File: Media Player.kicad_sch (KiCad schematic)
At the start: 71 parts, among them J1 PH2.0, J2 MEM2075-00-140-01-A, J3 USB_C_Receptacle_USB2.0_14P, J4 UART, Q2 DMP3068L-7, Q3 DMP3068L-7, SW1 BOOT, SW2 RESET, SW3 SW_Push, SW4 SW_Push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

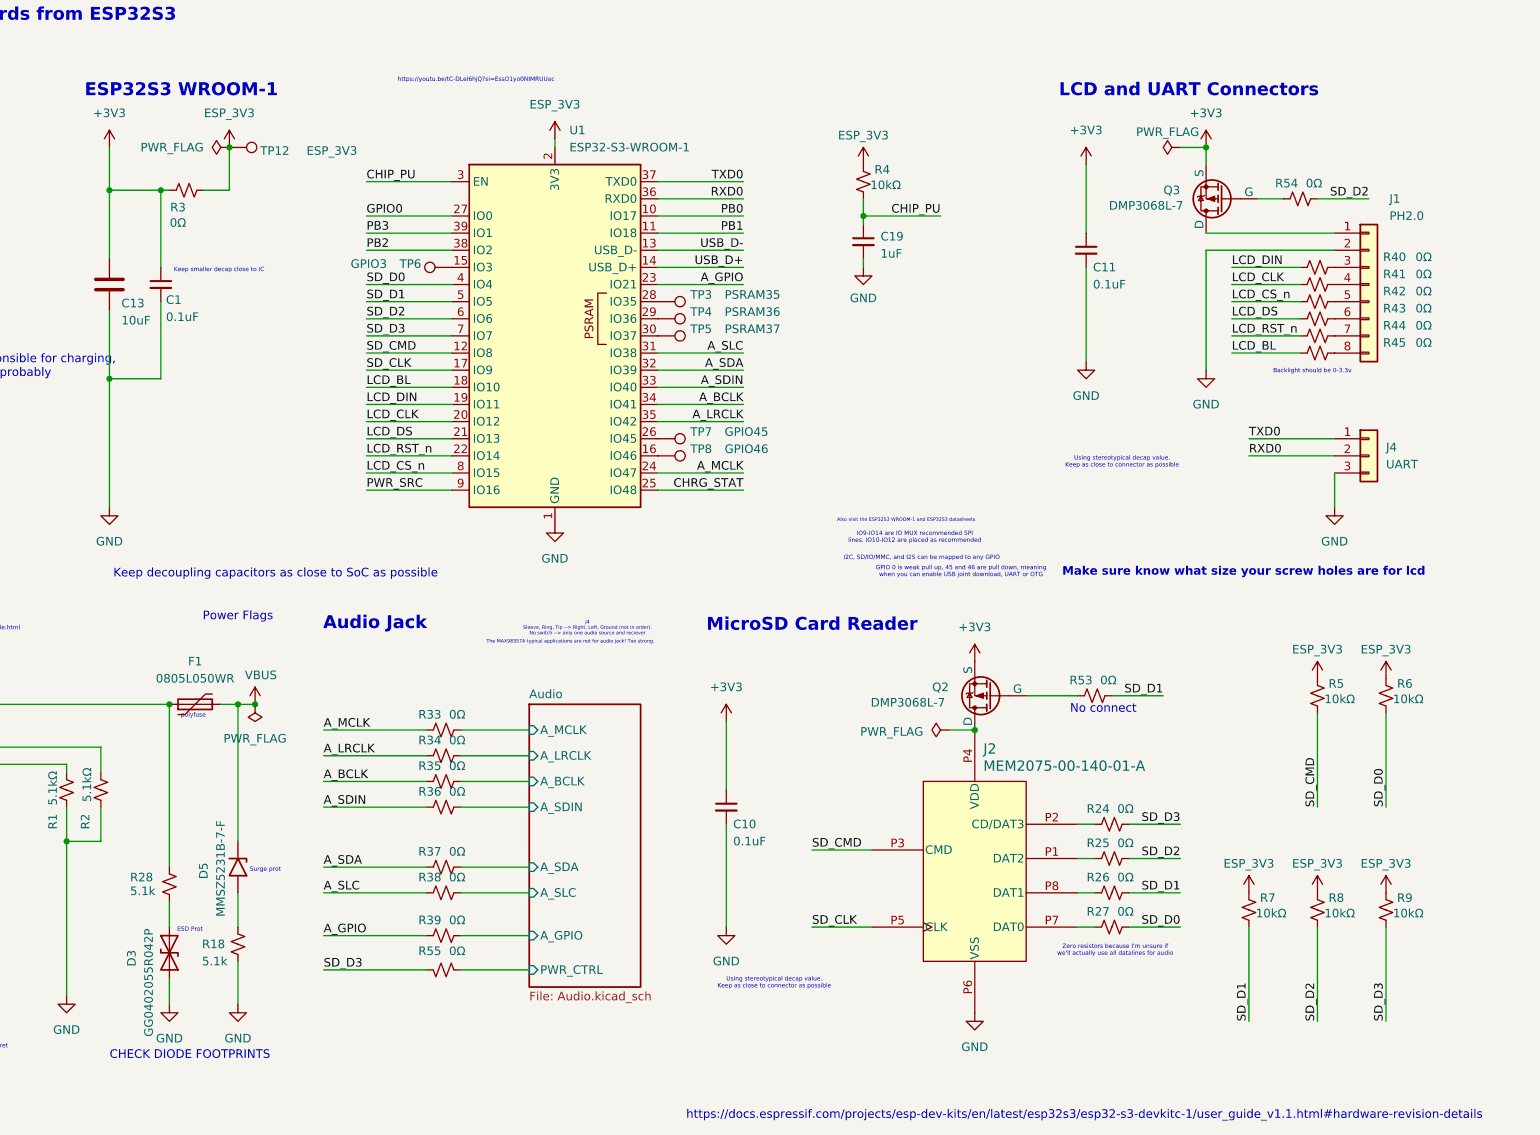
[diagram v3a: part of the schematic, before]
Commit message: Ratsnest organized
Certain pins on esp32 module changed to benefit layout. Named all decaps to dC. Current layout areas might be not optimal, i.e. complicated to wire
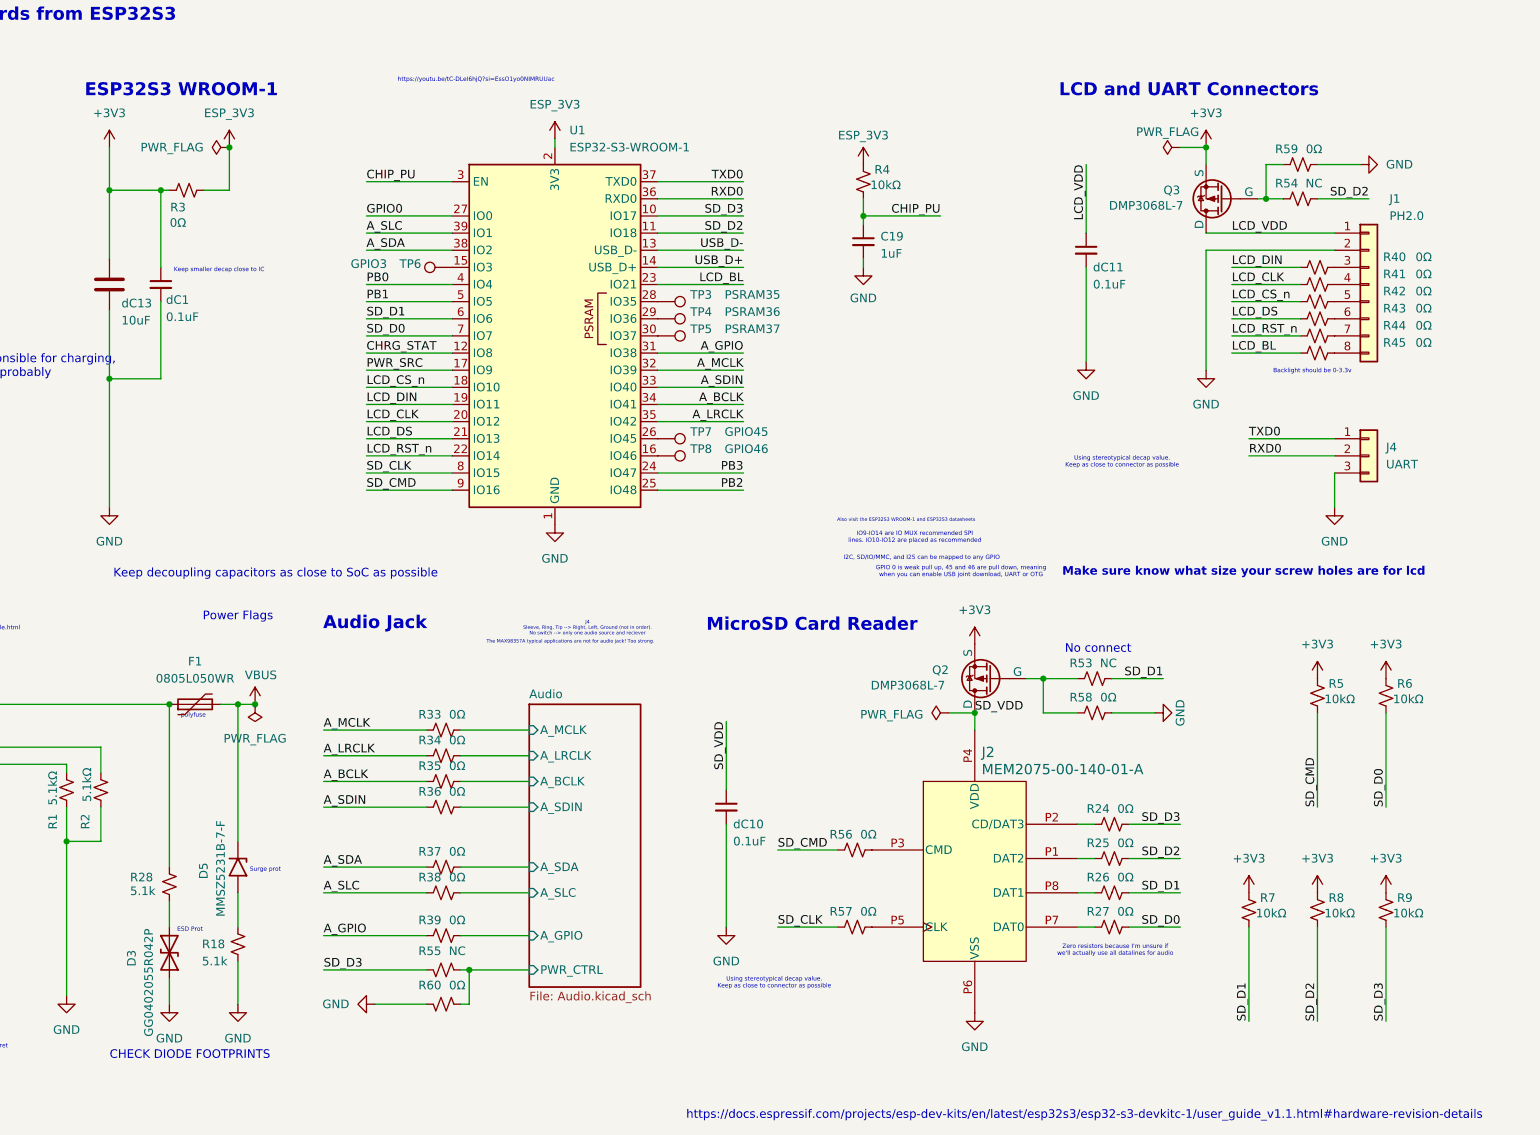
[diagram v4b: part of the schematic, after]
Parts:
- removed TP12: ESP_3V3, TestPoint:TestPoint_Pad_1.5x1.5mm, symbol Connector:TestPoint
- added R56, R57, R58, R59, R60: 0Ω, Resistor_SMD:R_0805_2012Metric, symbol Device:R_Small_US
- C19: footprint Capacitor_SMD:C_0805_2012Metric_Pad1.18x1.45mm_HandSolder -> Capacitor_SMD:C_0603_1608Metric_Pad1.08x0.95mm_HandSolder
- R53, R54, R55: value 0Ω -> NC
- dC1: renamed from C1; footprint Capacitor_SMD:C_0805_2012Metric_Pad1.18x1.45mm_HandSolder -> Capacitor_SMD:C_0603_1608Metric_Pad1.08x0.95mm_HandSolder
- dC10: renamed from C10; footprint Capacitor_SMD:C_0805_2012Metric_Pad1.18x1.45mm_HandSolder -> Capacitor_SMD:C_0603_1608Metric_Pad1.08x0.95mm_HandSolder
- dC11: renamed from C11; footprint Capacitor_SMD:C_0805_2012Metric_Pad1.18x1.45mm_HandSolder -> Capacitor_SMD:C_0603_1608Metric_Pad1.08x0.95mm_HandSolder
- dC13: renamed from C13; footprint Capacitor_SMD:C_0805_2012Metric_Pad1.18x1.45mm_HandSolder -> Capacitor_SMD:C_0603_1608Metric_Pad1.08x0.95mm_HandSolder
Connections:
- net +3V3: now also R5.2, R6.2, R7.2, R8.2, R9.2; no longer dC10.1, dC11.1
- net A_GPIO: now also U1.31 (IO38); no longer U1.23 (IO21)
- net A_MCLK: now also U1.32 (IO39); no longer U1.24 (IO47)
- net A_SDA: now also U1.38 (IO2); no longer U1.32 (IO39)
- net A_SLC: now also U1.39 (IO1); no longer U1.31 (IO38)
- net Audio/PWR_CTRL: now also R60.1
- net CHRG_STAT: now also U1.12 (IO8); no longer U1.25 (IO48)
- net ESP_3V3: no longer R5.2, R6.2, R7.2, R8.2, R9.2
- net GND: now also R58.2, R59.2, R60.2
- net LCD_BL: now also U1.23 (IO21); no longer U1.18 (IO10)
- net LCD_CS_n: now also U1.18 (IO10); no longer U1.8 (IO15)
- net PB0: now also U1.4 (IO4); no longer U1.10 (IO17)
- net PB1: now also U1.5 (IO5); no longer U1.11 (IO18)
- net PB2: now also U1.25 (IO48); no longer U1.38 (IO2)
- net PB3: now also U1.24 (IO47); no longer U1.39 (IO1)
- net PWR_SRC: now also U1.17 (IO9); no longer U1.9 (IO16)
- net SD_CLK: now also U1.8 (IO15), R57.1; no longer J2.P5 (CLK), U1.17 (IO9)
- net SD_CMD: now also U1.9 (IO16), R56.1; no longer J2.P3 (CMD), U1.12 (IO8)
- net SD_D0: now also U1.7 (IO7); no longer U1.4 (IO4)
- net SD_D1: now also U1.6 (IO6); no longer U1.5 (IO5)
- net SD_D2: now also U1.11 (IO18); no longer U1.6 (IO6)
- net SD_D3: now also U1.10 (IO17); no longer U1.7 (IO7)
- net SD_VDD: now reaches J2.P4 (VDD), Q2.1 (D)
- net SD_VDD: now also dC10.1
- net at Q2.2 (G), R53.1: now also R58.1
- net at Q3.2 (G), R54.1: now also R59.1
- net LCD_VDD: now reaches J1.1 (Pin_1), Q3.1 (D)
- net LCD_VDD: now also dC11.1
- new net: J2.P3 (CMD), R56.2
- new net: J2.P5 (CLK), R57.2
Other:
- moved on the sheet: Q2, R53

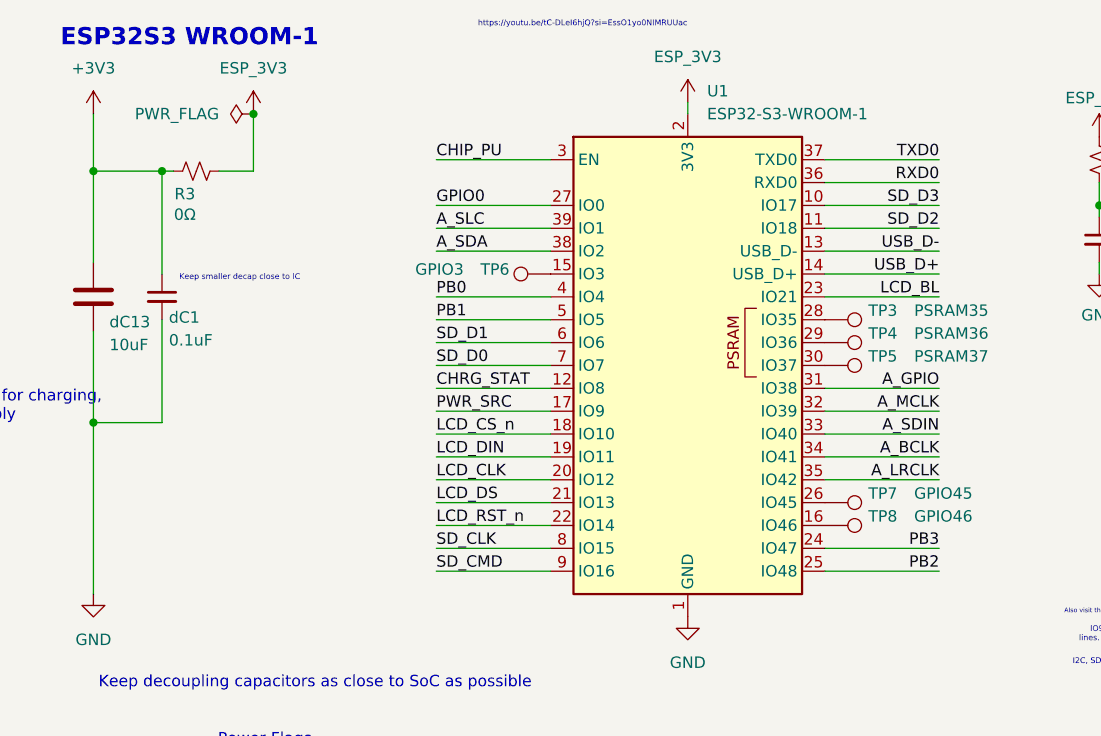
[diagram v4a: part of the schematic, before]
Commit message: Component Re-order
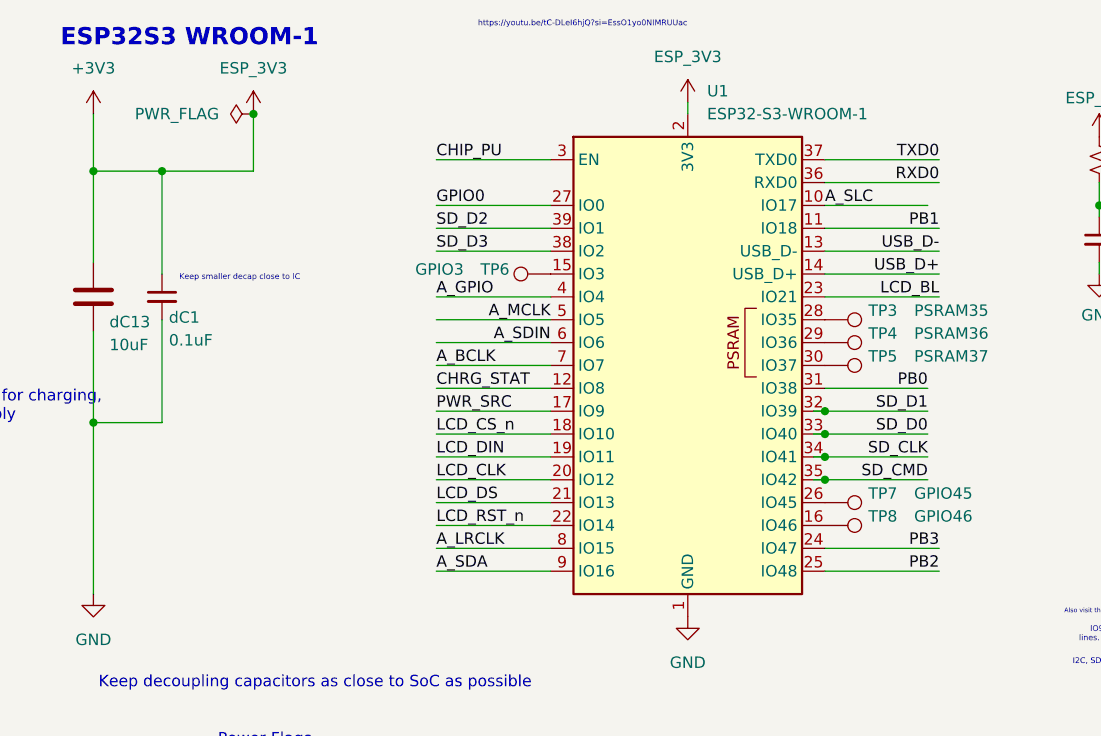
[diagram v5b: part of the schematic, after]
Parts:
- removed R3: 0Ω, Resistor_SMD:R_0805_2012Metric, symbol Device:R_Small_US
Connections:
- net ESP_3V3 is gone; now on net +3V3: R4.2, U1.2 (3V3)
- net A_BCLK: now also U1.7 (IO7); no longer U1.34 (IO41)
- net A_GPIO: now also U1.4 (IO4); no longer U1.31 (IO38)
- net A_LRCLK: now also U1.8 (IO15); no longer U1.35 (IO42)
- net A_MCLK: now also U1.5 (IO5); no longer U1.32 (IO39)
- net A_SDA: now also U1.9 (IO16); no longer U1.38 (IO2)
- net A_SDIN: now also U1.6 (IO6); no longer U1.33 (IO40)
- net A_SLC: now also U1.10 (IO17); no longer U1.39 (IO1)
- net PB0: now also U1.31 (IO38); no longer U1.4 (IO4)
- net PB1: now also U1.11 (IO18); no longer U1.5 (IO5)
- net SD_CLK: now also U1.34 (IO41); no longer U1.8 (IO15)
- net SD_CMD: now also U1.35 (IO42); no longer U1.9 (IO16)
- net SD_D0: now also U1.33 (IO40); no longer U1.7 (IO7)
- net SD_D1: now also U1.32 (IO39); no longer U1.6 (IO6)
- net SD_D2: now also U1.39 (IO1); no longer U1.11 (IO18)
- net SD_D3: now also U1.38 (IO2); no longer U1.10 (IO17)

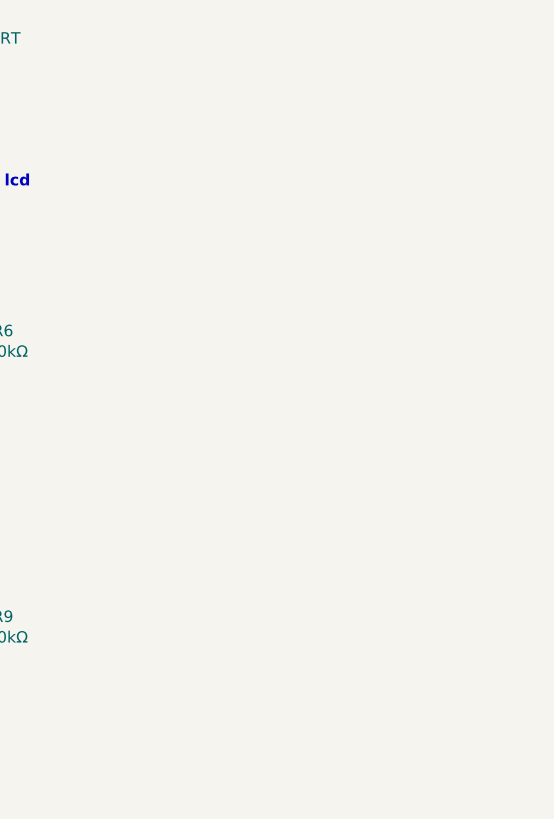
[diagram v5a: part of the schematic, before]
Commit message: Added alternative audio IC
Added a SOP package audio IC (for easier board bring up) in hopes to replace MAX9850. Pins not fully mapped yet.
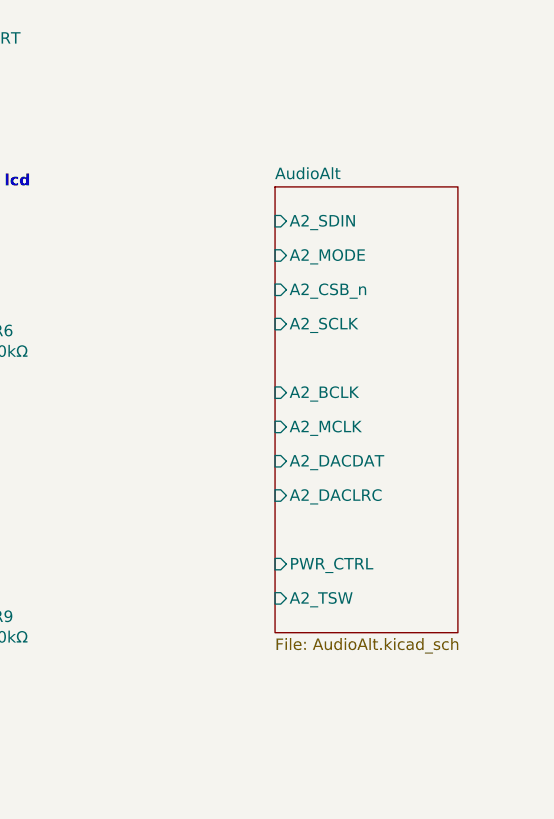
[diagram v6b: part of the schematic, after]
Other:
- added sheet AudioAlt (AudioAlt.kicad_sch)
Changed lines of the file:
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@@
+		)
+	)
+	(sheet
+		(at 307.34 90.17)
+		(size 20.32 49.53)
+		(exclude_from_sim no)
+		(in_bom yes)
+		(on_board yes)
+		(dnp no)
+		(fields_autoplaced yes)
+		(stroke
+			(width 0.1524)
+			(type solid)
+		)
+		(fill
+			(color 247 255 191 1.0000)
+		)
+		(property "Sheetname" "AudioAlt"
+			(at 307.34 89.4584 0)
+			(effects
+				(font
+					(size 1.27 1.27)
+				)
+				(justify left bottom)
+			)
+		)
+		(property "Sheetfile" "AudioAlt.kicad_sch"
+			(at 307.34 140.2846 0)
+			(effects
+				(font
+					(size 1.27 1.27)
+				)
+				(justify left top)
+			)
+		)
+		(pin "A2_SDIN" input
+			(at 307.34 93.98 180)
+			(effects
+				(font
+					(size 1.27 1.27)
+				)
+				(justify left)
+			)
+		)
+		(pin "A2_MODE" input
+			(at 307.34 97.79 180)
+			(effects
+				(font
+					(size 1.27 1.27)
+				)
+				(justify left)
+			)
+		)
+		(pin "A2_CSB_n" input
+			(at 307.34 101.6 180)
+			(effects
+				(font
+					(size 1.27 1.27)
+				)
+				(justify left)
+			)
+		)
+		(pin "A2_SCLK" input
+			(at 307.34 105.41 180)
+			(effects
+				(font
+					(size 1.27 1.27)
+				)
+				(justify left)
+			)
+		)
+		(pin "PWR_CTRL" input
+			(at 307.34 132.08 180)
+			(effects
+				(font
+					(size 1.27 1.27)
+				)
+				(justify left)
+			)
+		)
+		(pin "A2_MCLK" input
+			(at 307.34 116.84 180)
+			(effects
+				(font
+					(size 1.27 1.27)
+				)
+				(justify left)
+			)
+		)
+		(pin "A2_DACDAT" input
+			(at 307.34 120.65 180)
+			(effects
+				(font
+					(size 1.27 1.27)
+				)
+				(justify left)
+			)
+		)
+		(pin "A2_TSW" input
+			(at 307.34 135.89 180)
+			(effects
+				(font
+					(size 1.27 1.27)
+				)
+				(justify left)
+			)
+		)
+		(pin "A2_BCLK" input
+			(at 307.34 113.03 180)
+			(effects
+				(font
+					(size 1.27 1.27)
+				)
+				(justify left)
+			)
+		)
+		(pin "A2_DACLRC" input
+			(at 307.34 124.46 180)
+			(effects
+				(font
+					(size 1.27 1.27)
+				)
+				(justify left)
+			)
+		)
+		(instances
+			(project "Media Player"
+				(path "/5c19345b-3707-4c90-b593-78a9c3e56866"
+					(page "4")
+				)
+			)
 		)
 	)
